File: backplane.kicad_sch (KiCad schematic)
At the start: 7 parts, among them J5 Edge_Conn_HSEC8-120, U12 ESD204DQAR, U13 ESD204DQAR, U14 ESD204DQAR, U15 ESD204DQAR, U16 ESD204DQAR, U17 ESD204DQAR

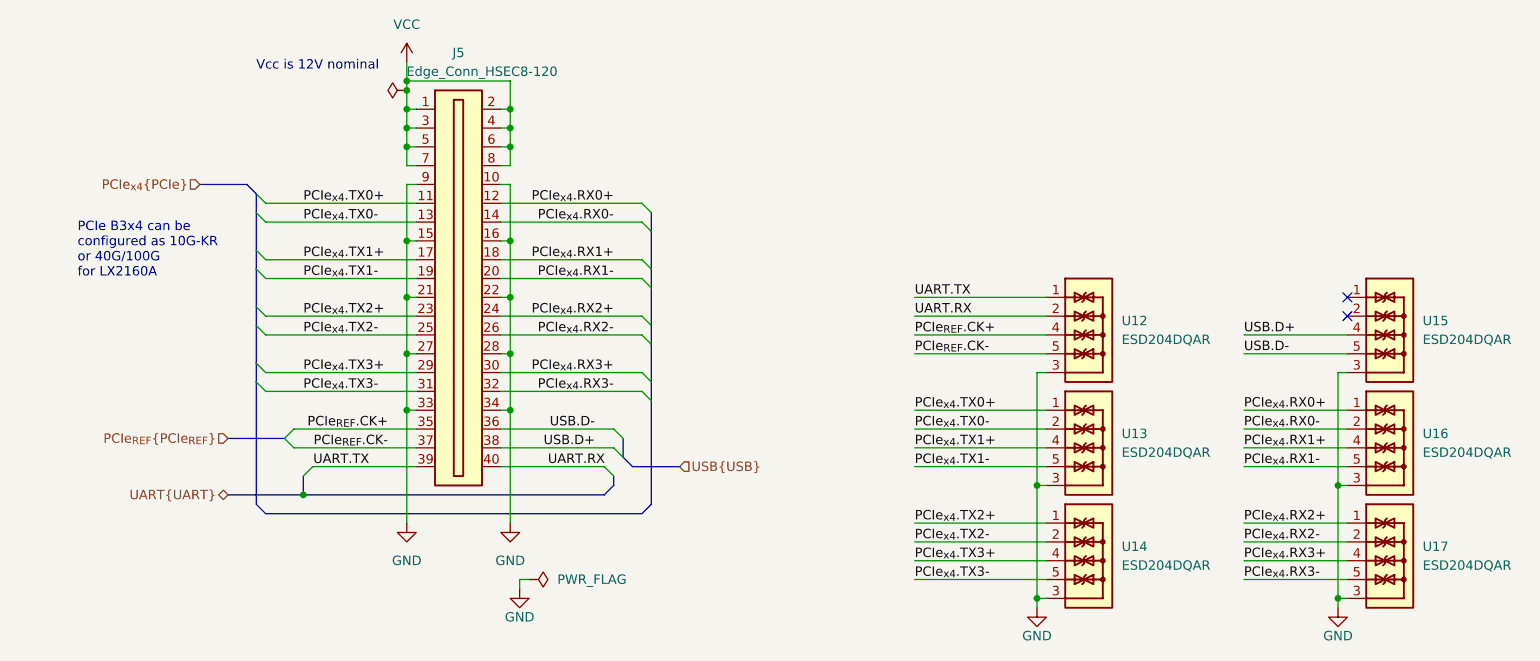
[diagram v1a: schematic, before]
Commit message: [#58904] Change pinout of backplane connector. Connect CLKREQ from PCIe devices
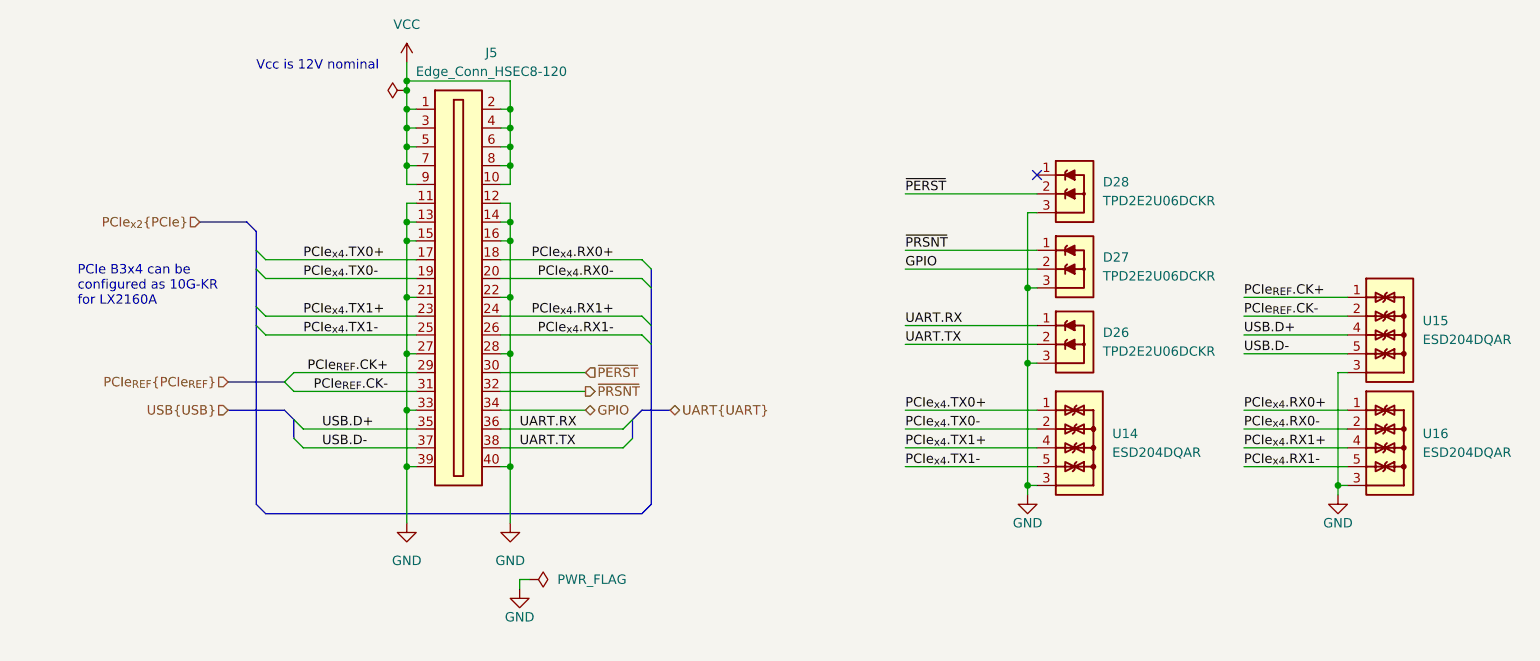
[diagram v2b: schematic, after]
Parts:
- removed U12, U13, U17: ESD204DQAR, antmicro-footprints:USON-10_2.5x1mm_P0.5mm, symbol antmicroTVSDiodes:ESD204DQAR
- added D26, D27, D28: TPD2E2U06DCKR, antmicro-footprints:SC70-3, symbol antmicroTVSDiodes:TPD2E2U06DCKR
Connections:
- net PCIe_{x4}.RX2+ is gone; now on net PCIe_{x4}.RX1+: J5.24
- net PCIe_{x4}.RX2- is gone; now on net PCIe_{x4}.RX1-: J5.26
- net GND: now also J5.11, J5.12, J5.13, J5.14, J5.39, J5.40, D26.3, D27.3, D28.3; no longer J5.10, J5.34, J5.9
- net PCIe_{REF}.CK+: now also J5.29, U15.1, U15.10; no longer J5.35
- net PCIe_{REF}.CK-: now also J5.31, U15.2, U15.9; no longer J5.37
- net PCIe_{x4}.RX0+: now also J5.18; no longer J5.12
- net PCIe_{x4}.RX0-: now also J5.20; no longer J5.14
- net PCIe_{x4}.RX1+: no longer J5.18
- net PCIe_{x4}.RX1-: no longer J5.20
- net PCIe_{x4}.TX0+: now also J5.17, U14.1, U14.10; no longer J5.11
- net PCIe_{x4}.TX0-: now also J5.19, U14.2, U14.9; no longer J5.13
- net PCIe_{x4}.TX1+: now also J5.23, U14.4, U14.7; no longer J5.17
- net PCIe_{x4}.TX1-: now also J5.25, U14.5, U14.6; no longer J5.19
- net UART.RX: now also J5.36, D26.1; no longer J5.40
- net UART.TX: now also J5.38, D26.2; no longer J5.39
- net USB.D+: now also J5.35; no longer J5.38
- net USB.D-: now also J5.37; no longer J5.36
- net VCC: now also J5.10, J5.9
- net PCIe_{x4}.RX3+ renamed ~{PERST}
- net ~{PERST}: now also D28.2
- net PCIe_{x4}.RX3- renamed ~{PRSNT}
- net ~{PRSNT}: now also D27.1
- removed net PCIe_{x4}.TX2+: J5.23, U14.1, U14.10
- removed net PCIe_{x4}.TX2-: J5.25, U14.2, U14.9
- removed net PCIe_{x4}.TX3+: J5.29, U14.4, U14.7
- removed net PCIe_{x4}.TX3-: J5.31, U14.5, U14.6
- new net GPIO: D27.2, J5.34
- no-connect marks 2 -> 1
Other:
- note added: "PCIe B3x4 can be configured as 10G-KR for LX2160A"
- note removed: "PCIe B3x4 can be configured as 10G-KR or 40G/100G for LX2160A"
- moved on the sheet: U14

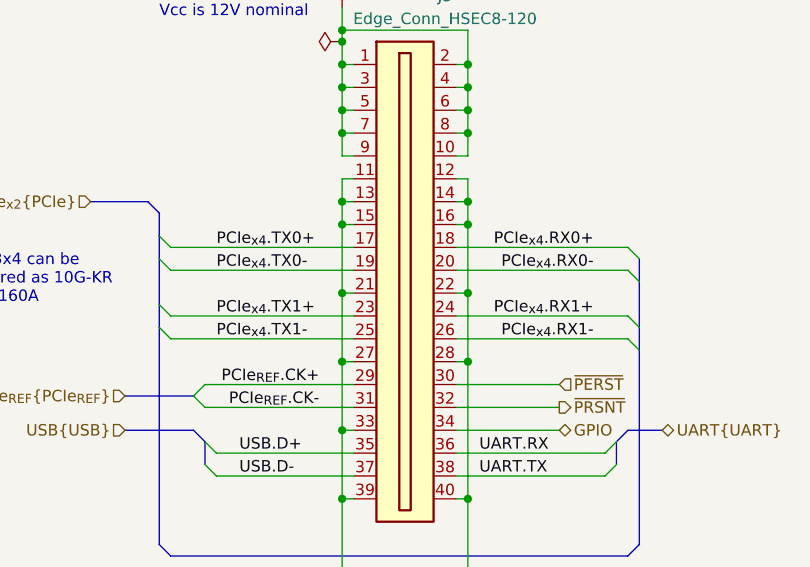
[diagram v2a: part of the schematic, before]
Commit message: [#58904] Fix DRC
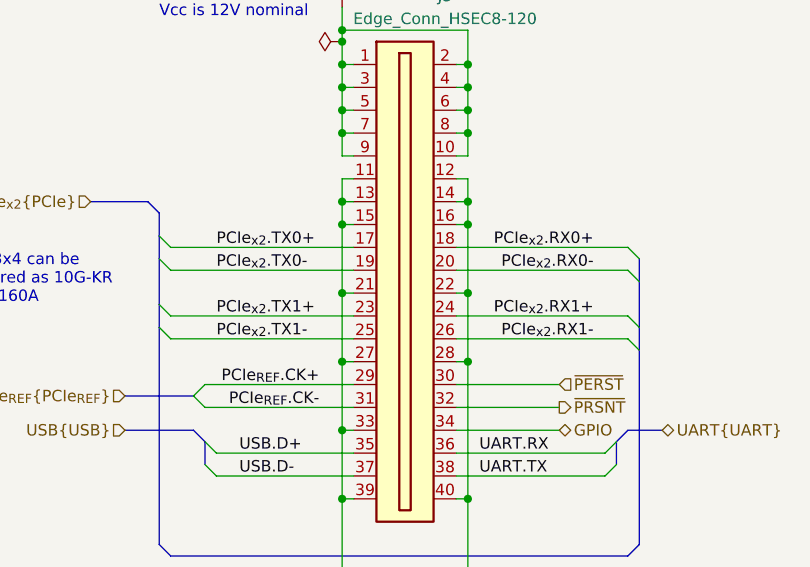
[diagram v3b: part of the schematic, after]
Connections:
- net PCIe_{x4}.RX0+: no longer J5.18
- net PCIe_{x4}.RX0-: no longer J5.20
- net PCIe_{x4}.RX1+: no longer J5.24
- net PCIe_{x4}.RX1-: no longer J5.26
- net PCIe_{x4}.TX0+: no longer J5.17
- net PCIe_{x4}.TX0-: no longer J5.19
- net PCIe_{x4}.TX1+: no longer J5.23
- net PCIe_{x4}.TX1-: no longer J5.25
- new net PCIe_{x2}.RX0+: J5.18
- new net PCIe_{x2}.RX0-: J5.20
- new net PCIe_{x2}.RX1+: J5.24
- new net PCIe_{x2}.RX1-: J5.26
- new net PCIe_{x2}.TX0+: J5.17
- new net PCIe_{x2}.TX0-: J5.19
- new net PCIe_{x2}.TX1+: J5.23
- new net PCIe_{x2}.TX1-: J5.25
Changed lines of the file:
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@@
     (effects (font (size 1.27 1.27)) (justify left bottom))
   )
-  (label "PCIe_{x4}.TX1-" (at 176.53 154.94 0) (fields_autoplaced)
+  (label "PCIe_{x2}.TX1-" (at 176.53 154.94 0) (fields_autoplaced)
     (effects (font (size 1.27 1.27)) (justify left bottom))
   )
-  (label "PCIe_{x4}.RX1+" (at 218.44 152.4 180) (fields_autoplaced)
+  (label "PCIe_{x2}.RX1+" (at 218.44 152.4 180) (fields_autoplaced)
     (effects (font (size 1.27 1.27)) (justify right bottom))
   )
@@
     (effects (font (size 1.27 1.27)) (justify left bottom))
   )
-  (label "PCIe_{x4}.RX0+" (at 218.44 144.78 180) (fields_autoplaced)
+  (label "PCIe_{x2}.RX0+" (at 218.44 144.78 180) (fields_autoplaced)
     (effects (font (size 1.27 1.27)) (justify right bottom))
   )
@@
     (effects (font (size 1.27 1.27)) (justify left bottom))
   )
-  (label "PCIe_{x4}.RX1-" (at 218.44 154.94 180) (fields_autoplaced)
+  (label "PCIe_{x2}.RX1-" (at 218.44 154.94 180) (fields_autoplaced)
     (effects (font (size 1.27 1.27)) (justify right bottom))
   )
@@
     (effects (font (size 1.27 1.27)) (justify left bottom))
   )
-  (label "PCIe_{x4}.RX0-" (at 218.44 147.32 180) (fields_autoplaced)
+  (label "PCIe_{x2}.RX0-" (at 218.44 147.32 180) (fields_autoplaced)
     (effects (font (size 1.27 1.27)) (justify right bottom))
   )
@@
     (effects (font (size 1.27 1.27)) (justify left bottom))
   )
-  (label "PCIe_{x4}.TX1+" (at 176.53 152.4 0) (fields_autoplaced)
+  (label "PCIe_{x2}.TX1+" (at 176.53 152.4 0) (fields_autoplaced)
     (effects (font (size 1.27 1.27)) (justify left bottom))
   )
-  (label "PCIe_{x4}.TX0-" (at 176.53 147.32 0) (fields_autoplaced)
+  (label "PCIe_{x2}.TX0-" (at 176.53 147.32 0) (fields_autoplaced)
     (effects (font (size 1.27 1.27)) (justify left bottom))
   )
@@
     (effects (font (size 1.27 1.27)) (justify left bottom))
   )
-  (label "PCIe_{x4}.TX0+" (at 176.53 144.78 0) (fields_autoplaced)
+  (label "PCIe_{x2}.TX0+" (at 176.53 144.78 0) (fields_autoplaced)
     (effects (font (size 1.27 1.27)) (justify left bottom))
   )

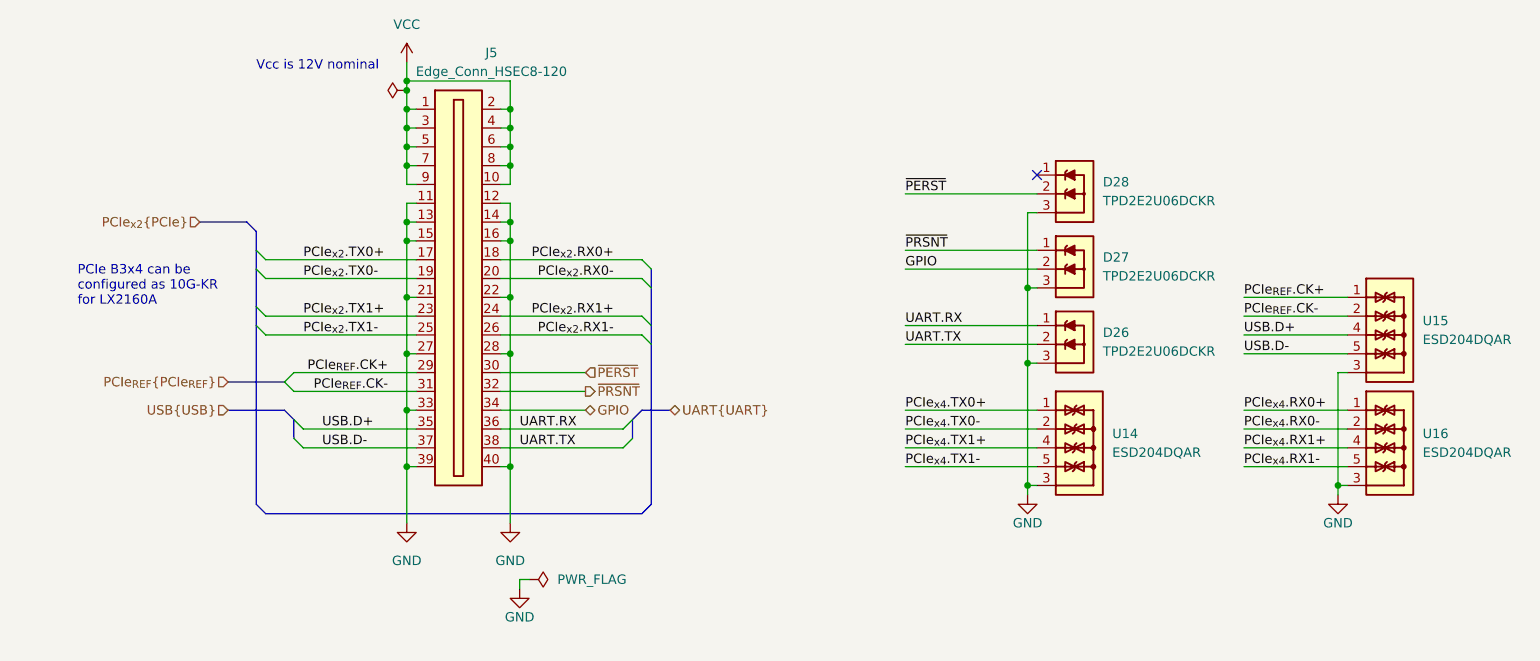
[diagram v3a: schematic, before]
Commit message: Update components from the library
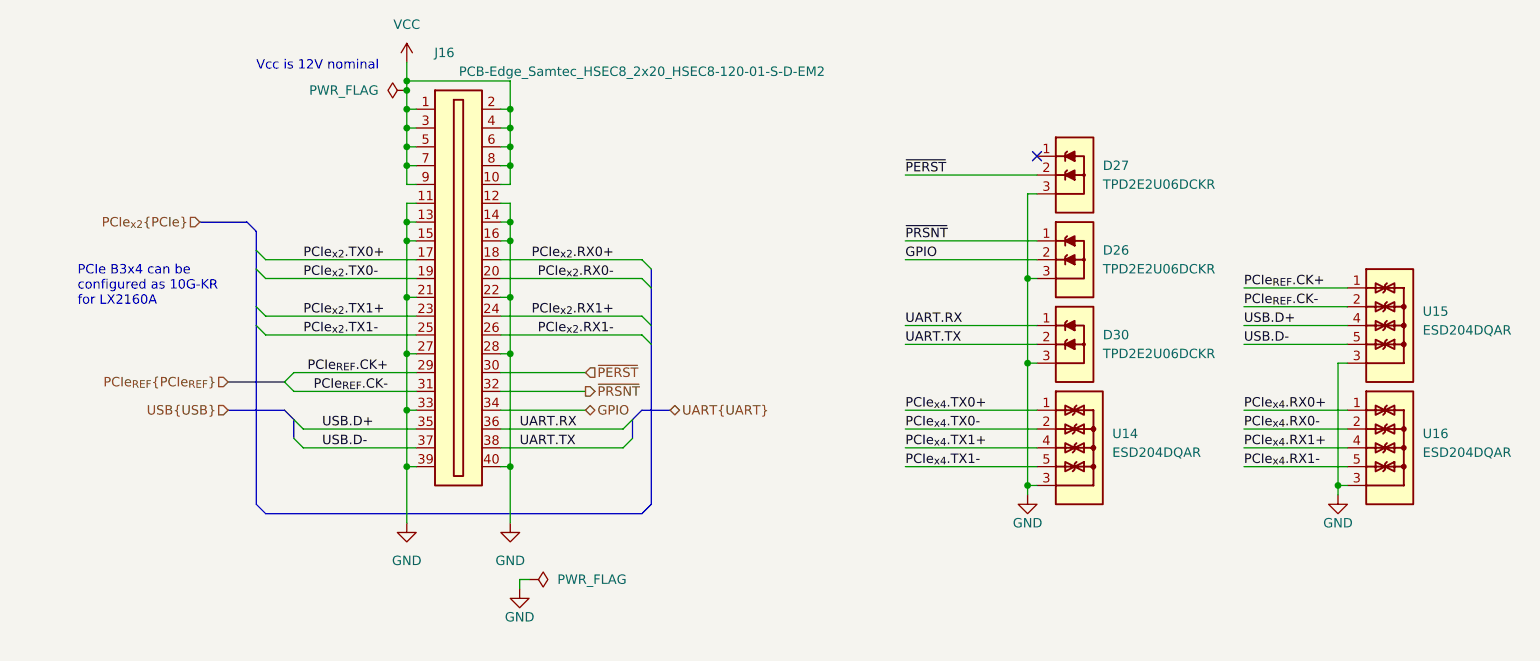
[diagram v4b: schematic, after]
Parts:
- removed D26, D27, D28: TPD2E2U06DCKR, antmicro-footprints:SC70-3, symbol antmicroTVSDiodes:TPD2E2U06DCKR
- removed J5: Edge_Conn_HSEC8-120, antmicro-footprints:Edge_Conn_HSEC8_120, symbol antmicroEdgeConnectors:Edge_Conn_HSEC8-120
- added D26, D27, D30: TPD2E2U06_SC70, antmicro-footprints:SC70-3, symbol antmicroTVSDiodes:TPD2E2U06_SC70
- added J16: PCB-Edge_Samtec_HSEC8_2x20_HSEC8-120-01-S-D-EM2, antmicro-footprints:PCB-Edge_Samtec_HSEC8_2x20_HSEC8-120-01-S-D-EM2, symbol antmicroEdgeConnectors:PCB-Edge_Samtec_HSEC8_2x20_HSEC8-120-01-S-D-EM2
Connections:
- net GND: now also D26.3, D27.3, D30.3, J16.11, J16.12, J16.13, J16.14, J16.15, J16.16, J16.21, J16.22, J16.27, J16.28, J16.33, J16.39, J16.40
- net GPIO: now also D26.2, J16.34
- net PCIe_{REF}.CK+: now also J16.29
- net PCIe_{REF}.CK-: now also J16.31
- net PCIe_{x2}.RX0+: now also J16.18
- net PCIe_{x2}.RX0-: now also J16.20
- net PCIe_{x2}.RX1+: now also J16.24
- net PCIe_{x2}.RX1-: now also J16.26
- net PCIe_{x2}.TX0+: now also J16.17
- net PCIe_{x2}.TX0-: now also J16.19
- net PCIe_{x2}.TX1+: now also J16.23
- net PCIe_{x2}.TX1-: now also J16.25
- net UART.RX: now also D30.1, J16.36
- net UART.TX: now also D30.2, J16.38
- net USB.D+: now also J16.35
- net USB.D-: now also J16.37
- net VCC: now also J16.1, J16.10, J16.2, J16.3, J16.4, J16.5, J16.6, J16.7, J16.8, J16.9
- net ~{PERST}: now also D27.2, J16.30
- net ~{PRSNT}: now also D26.1, J16.32
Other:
- moved on the sheet: U14, U15, U16

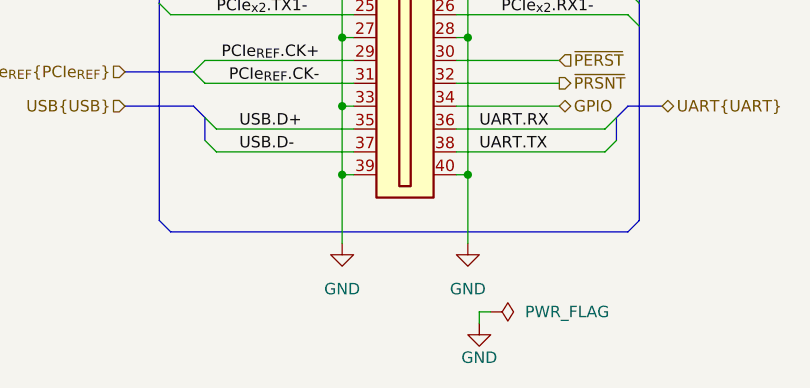
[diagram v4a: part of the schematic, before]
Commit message: [#65447] Fix rotated LEDs, overlapping text and symbols, add rules
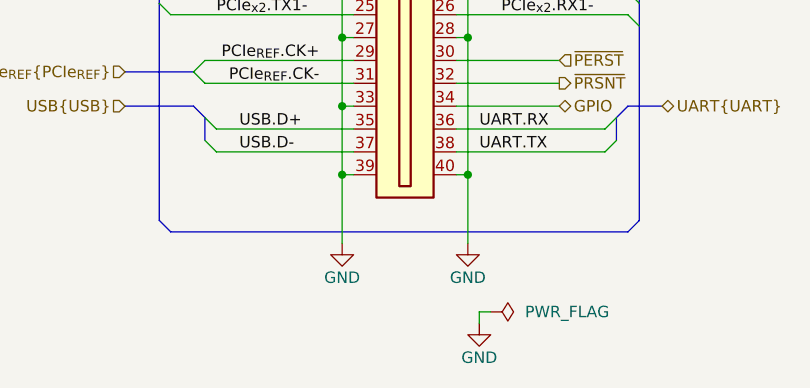
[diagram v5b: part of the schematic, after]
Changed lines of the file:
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@@
   )
   (symbol (lib_id "antmicropower:GND") (at 190.5 180.34 0) (unit 1)
-    (in_bom yes) (on_board yes) (dnp no) (fields_autoplaced)
+    (in_bom yes) (on_board yes) (dnp no)
     (property "Reference" "#PWR081" (at 199.39 182.88 0)
       (effects (font (size 1.27 1.27) (thickness 0.15)) (justify left bottom) hide)
     )
-    (property "Value" "GND" (at 190.5 185.42 0)
+    (property "Value" "GND" (at 190.5 184.15 0)
       (effects (font (size 1.27 1.27) (thickness 0.15)))
     )
@@
   )
   (symbol (lib_id "antmicropower:GND") (at 204.47 180.34 0) (unit 1)
-    (in_bom yes) (on_board yes) (dnp no) (fields_autoplaced)
+    (in_bom yes) (on_board yes) (dnp no)
     (property "Reference" "#PWR082" (at 213.36 182.88 0)
       (effects (font (size 1.27 1.27) (thickness 0.15)) (justify left bottom) hide)
     )
-    (property "Value" "GND" (at 204.47 185.42 0)
+    (property "Value" "GND" (at 204.47 184.15 0)
       (effects (font (size 1.27 1.27) (thickness 0.15)))
     )
